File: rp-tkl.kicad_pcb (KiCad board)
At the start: 2 copper layers, 344.7 x 123.1 mm, 228 parts, among them J1 USB_C_Receptacle_USB2.0, J2 SWD, SW1 SW_Push, SW10 ?, SW100 ?, SW101 ?, SW102 ?, SW103 ?, SW104 ?, SW105 ?, SW11 ?, SW12 ?, SW13 ?, SW14 ?, SW15 ?, SW16 ?, SW17 ?, SW18 ?, SW19 ?, SW2 ?, SW20 ?, SW21 ?, SW22 ?, SW23 ?, SW24 ?, SW25 ?, SW26 ?, SW27 ?, SW28 ?, SW29 ?, SW3 ?, SW30 ?, SW31 ?, SW32 ?, SW33 ?, SW34 ?, SW35 ?, SW36 ?, SW37 ?, SW38 ?, SW39 ?, SW4 ?, SW40 ?, SW41 ?, SW42 ?, SW43 ?, SW44 ?, SW45 ?, SW46 ?, SW47 ?, SW48 ?, SW49 ?, SW5 ?, SW50 ?, SW51 ?, SW52 ?, SW53 ?, SW54 ?, SW55 ?, SW56 ?, SW57 ?, SW58 ?, SW59 ?, SW6 ?, SW60 ?, SW61 ?, SW62 ?, SW63 ?, SW64 ?, SW65 ?, SW66 ?, SW67 ?, SW68 ?, SW69 ?, SW7 ?, SW70 ?, SW71 ?, SW72 ?, SW73 ?, SW74 ?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

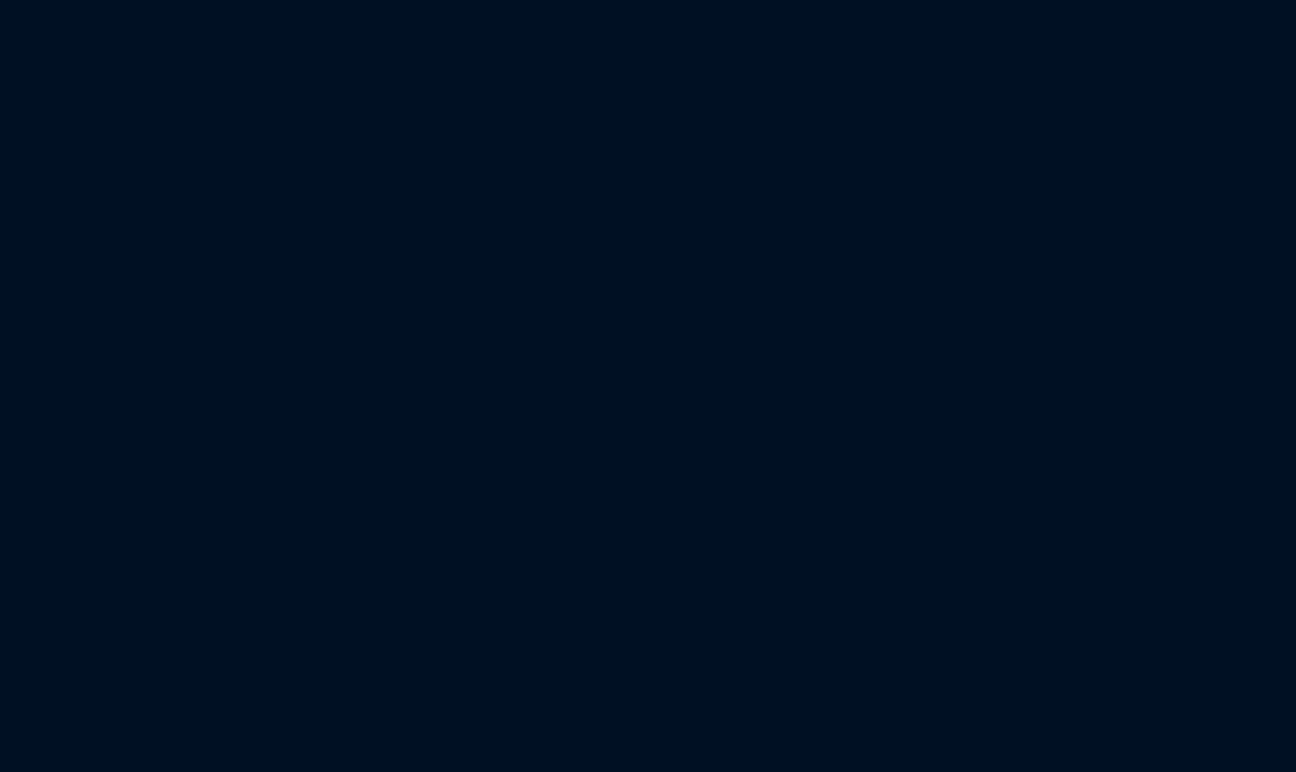
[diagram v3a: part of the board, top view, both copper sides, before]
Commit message: Added Stabilizers
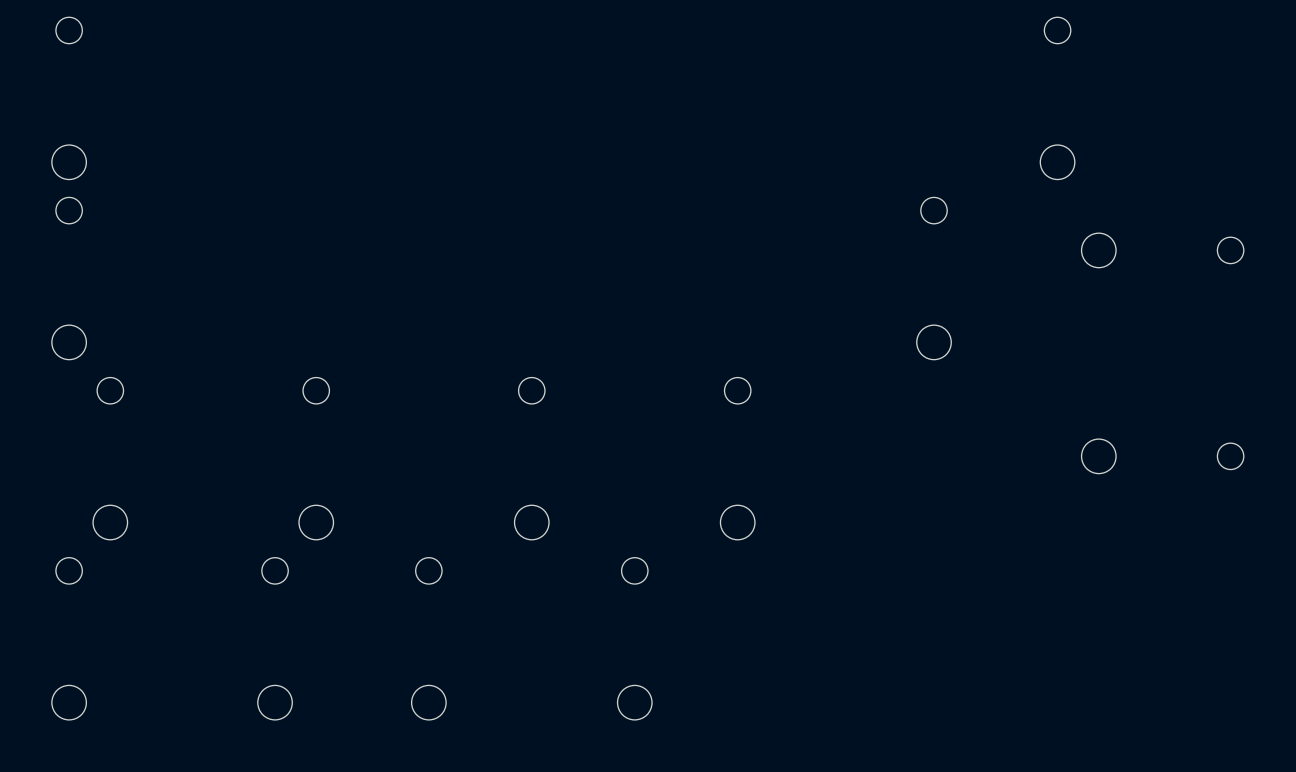
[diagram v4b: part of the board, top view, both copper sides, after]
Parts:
- added S1: BACKSPACE, marbastlib-mx:STAB_MX_2u, F.Cu at (544.9, 24.8)
- added S2: ISO_ENTER, marbastlib-mx:STAB_MX_ISO_FLIPPED, F.Cu at (618.7, -7.31)
- added S3: ANSI_ENTER, marbastlib-mx:STAB_MX_2.25u, F.Cu at (556.8, 3.99)
- added S4: LSHIFT, marbastlib-mx:STAB_MX_2.25u, F.Cu at (503.3, 24.8)
- added S5: RSHIFT, marbastlib-mx:STAB_MX_2.75u, F.Cu at (508.1, 3.99)
- added S6: 7U_SPACE, marbastlib-mx:STAB_MX_7u, F.Cu at (548.6, -37.7)
- added S7: 6.25U_SPACE, marbastlib-mx:STAB_MX_6.25u, F.Cu at (541.4, -16.8)

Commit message: All switches (not diodes) in position
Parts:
- SW100: renamed from SW101; footprint marbastlib-mx:SW_MX_HS_1u -> marbastlib-mx:SW_MX_HS_1.5u
- SW101: renamed from SW102; footprint marbastlib-mx:SW_MX_HS_1u -> marbastlib-mx:SW_MX_HS_1.25u
- SW37: renamed from SW38; footprint marbastlib-mx:SW_MX_HS_1u -> marbastlib-mx:SW_MX_HS_1.5u
- SW50: renamed from SW51; footprint marbastlib-mx:SW_MX_HS_1u -> marbastlib-mx:SW_MX_HS_1.5u
- SW55: renamed from SW56; footprint marbastlib-mx:SW_MX_HS_1u -> marbastlib-mx:SW_MX_HS_1.75u_stp
- SW56: renamed from SW57; footprint marbastlib-mx:SW_MX_HS_1u -> marbastlib-mx:SW_MX_HS_1.75u
- SW70: renamed from SW71; footprint marbastlib-mx:SW_MX_HS_1u -> marbastlib-mx:SW_MX_HS_1.25u
- SW83: renamed from SW84; footprint marbastlib-mx:SW_MX_HS_1u -> marbastlib-mx:SW_MX_HS_1.75u
- SW87: renamed from SW88; footprint marbastlib-mx:SW_MX_HS_1u -> marbastlib-mx:SW_MX_HS_1.25u
- SW88: renamed from SW89; footprint marbastlib-mx:SW_MX_HS_1u -> marbastlib-mx:SW_MX_HS_1.5u
- SW89: renamed from SW90; footprint marbastlib-mx:SW_MX_HS_1u -> marbastlib-mx:SW_MX_HS_1.25u
- SW91: renamed from SW92; footprint marbastlib-mx:SW_MX_HS_1u -> marbastlib-mx:SW_MX_HS_1.25u
- SW92: renamed from SW93; footprint marbastlib-mx:SW_MX_HS_1u -> marbastlib-mx:SW_MX_HS_1.5u
- SW95: renamed from SW96; footprint marbastlib-mx:SW_MX_HS_1u -> marbastlib-mx:SW_MX_HS_1.25u
- SW96: renamed from SW97; footprint marbastlib-mx:SW_MX_HS_1u -> marbastlib-mx:SW_MX_HS_1.5u
- SW97: renamed from SW98; footprint marbastlib-mx:SW_MX_HS_1u -> marbastlib-mx:SW_MX_HS_1.25u
- SW99: renamed from SW100; footprint marbastlib-mx:SW_MX_HS_1u -> marbastlib-mx:SW_MX_HS_1.25u
- moved SW71 682.4 mm to (59.1, 146.3), turned to 0 degrees
- moved SW90 669.1 mm to (75.8, 165.3), turned to 0 degrees
- moved SW72 631.7 mm to (71.1, 146.3)
- moved SW59 621.8 mm to (118.7, 127.2)
- moved SW21 617.3 mm to (104.4, 89.1)
- moved SW91 604.6 mm to (97.2, 165.3)
- moved SW2 601.8 mm to (71.1, 65.3)
- moved SW6 591.7 mm to (152.0, 65.3)
- moved SW20 587.1 mm to (85.3, 89.1)
- moved SW57 582.2 mm to (80.6, 127.2)
- moved SW76 574.7 mm to (147.3, 146.3)
- moved SW56 571.1 mm to (54.4, 127.2), turned to 0 degrees
- moved SW39 565.3 mm to (94.9, 108.2)
- moved SW94 559.9 mm to (180.6, 165.3), turned to 0 degrees
- moved SW55 555.9 mm to (49.6, 127.2)
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- renumbered S7 to S6, S6 to S7, SW1 to SW0, SW2 to SW1, SW11 to SW10, SW103 to SW102, SW104 to SW103, SW105 to SW104, SW12 to SW11, SW13 to SW12, SW14 to SW13, SW15 to SW14, SW16 to SW15, SW17 to SW16, SW18 to SW17, SW19 to SW18, SW20 to SW19, SW3 to SW2, SW21 to SW20, SW22 to SW21, SW23 to SW22, SW24 to SW23, SW25 to SW24, SW26 to SW25, SW27 to SW26, SW28 to SW27, SW29 to SW28, SW30 to SW29, SW4 to SW3, SW31 to SW30, SW32 to SW31, SW33 to SW32, SW34 to SW33, SW35 to SW34, SW36 to SW35, SW37 to SW36, SW39 to SW38, SW40 to SW39, SW5 to SW4, SW41 to SW40, SW42 to SW41, SW43 to SW42, SW44 to SW43, SW45 to SW44, SW46 to SW45, SW47 to SW46, SW48 to SW47, SW49 to SW48, SW50 to SW49, SW6 to SW5, SW52 to SW51, SW53 to SW52, SW54 to SW53, SW55 to SW54, SW58 to SW57, SW59 to SW58, SW60 to SW59, SW7 to SW6, SW61 to SW60, SW62 to SW61, SW63 to SW62, SW64 to SW63, SW65 to SW64, SW66 to SW65, SW67 to SW66, SW68 to SW67, SW69 to SW68, SW70 to SW69, SW8 to SW7, SW72 to SW71, SW73 to SW72, SW74 to SW73, SW75 to SW74, SW76 to SW75, SW77 to SW76, SW78 to SW77, SW79 to SW78, SW80 to SW79, SW9 to SW8, SW81 to SW80, SW82 to SW81, SW83 to SW82, SW85 to SW84, SW86 to SW85, SW87 to SW86, SW10 to SW9, SW91 to SW90, SW94 to SW93, SW95 to SW94, SW99 to SW98

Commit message: [Preliminary] Positioned diodes
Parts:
- D1, D10, D11, D12, D13, D14, D15, D16, D17, D18, D19, D2, D20, D21, D22, D23, D24, D25, D26, D27, D28, D29, D3, D30, D31, D32, D33, D34, D35, D36, D37, D38, D39, D4, D40, D41, D42, D43, D44, D45, D46, D47, D48, D49, D5, D50, D51, D52, D53, D54, D55, D56, D57, D58, D59, D6, D60, D61, D62, D63, D64, D65, D66, D67, D68, D69, D7, D70, D71, D72, D73, D74, D75, D76, D77, D78, D79, D8, D80, D81, D82, D83, D84, D85, D86, D87, D88, D89, D9, D90, D91: footprint Diode_SMD:D_0402_1005Metric -> Diode_SMD:D_SOD-123
- moved D18 705.5 mm to (50.4, 89.9), turned to 90 degrees
- moved D1 659.9 mm to (50.4, 66.1), turned to 90 degrees
- moved D67 658.0 mm to (79.0, 146.2), turned to 90 degrees
- moved D37 655.5 mm to (79.0, 109.0), turned to 90 degrees
- moved D3 642.8 mm to (93.3, 66.1), turned to 90 degrees
- moved D53 633.2 mm to (60.7, 124.0)
- moved D83 630.6 mm to (107.6, 162.1), turned to -90 degrees
- moved D2 624.4 mm to (74.2, 66.1), turned to 90 degrees
- moved D54 616.3 mm to (83.8, 128.0), turned to 90 degrees
- moved D6 613.0 mm to (155.2, 66.1), turned to 90 degrees
- moved D68 609.9 mm to (93.3, 147.1), turned to 90 degrees
- moved D5 609.3 mm to (131.4, 66.1), turned to 90 degrees
- moved D24 600.4 mm to (164.7, 89.9), turned to 90 degrees
- moved D69 600.4 mm to (112.3, 147.1), turned to 90 degrees
- moved D38 600.1 mm to (98.0, 109.0), turned to 90 degrees
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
